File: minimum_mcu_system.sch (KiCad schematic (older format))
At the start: 0 parts

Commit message: resizing componentf
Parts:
- added U?: Stm8_my, symbol New_Schematic_Library:Stm8_my
- added Y?: Crystal, symbol Device:Crystal
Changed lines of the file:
@@
 Comment4 ""
 $EndDescr
+$Comp
+L New_Schematic_Library:Stm8_my U?
+U 1 1 606ACFA7
+P 5000 3550
+F 0 "U?" H 5008 4375 50  0000 C CNN
+F 1 "Stm8_my" H 5008 4284 50  0000 C CNN
+F 2 "" H 4550 4200 50  0001 C CNN
+F 3 "" H 4550 4200 50  0001 C CNN
+	1    5000 3550
+	1    0    0    -1
+$EndComp
+$Comp
+L Device:Crystal Y?
+U 1 1 606AE228
+P 3450 4050
+F 0 "Y?" V 3404 4181 50  0000 L CNN
+F 1 "Crystal" V 3495 4181 50  0000 L CNN
+F 2 "" H 3450 4050 50  0001 C CNN
+F 3 "~" H 3450 4050 50  0001 C CNN
+	1    3450 4050
+	0    1    1    0
+$EndComp
 $EndSCHEMATC

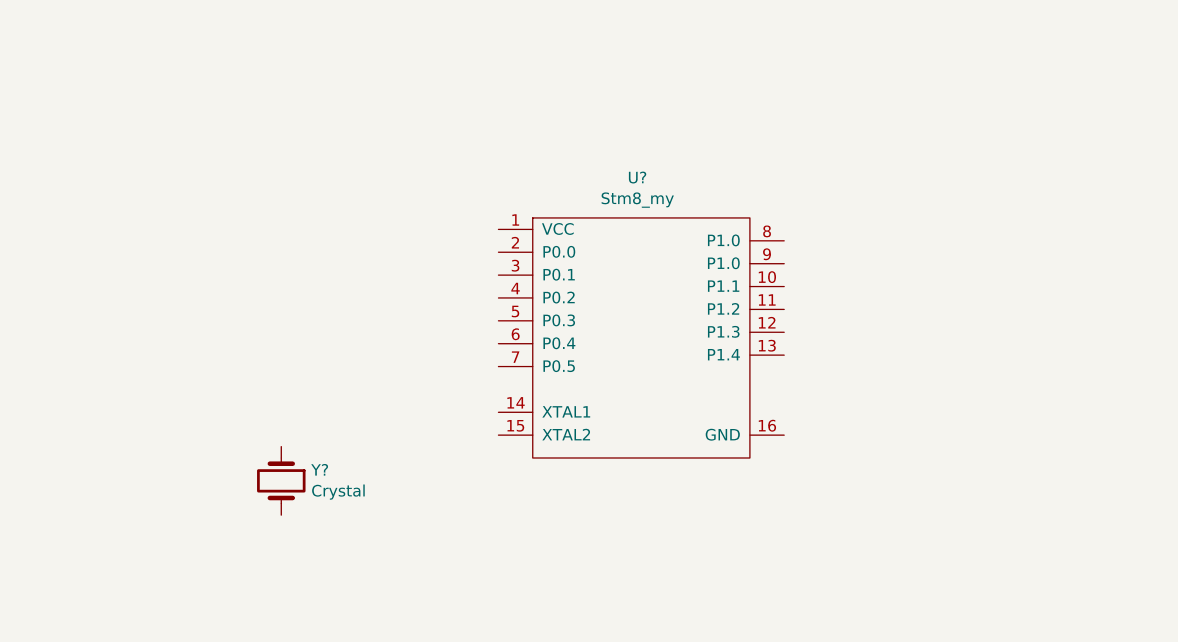
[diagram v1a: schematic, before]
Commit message: Added 3 capacitors,a cristal,an LED and a power input
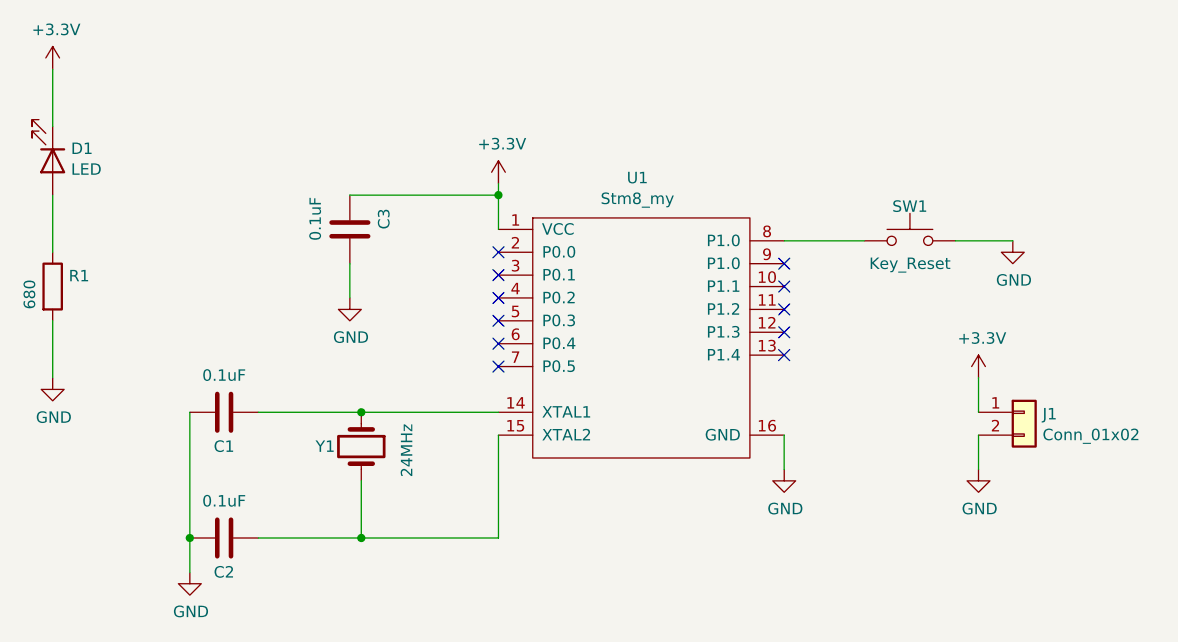
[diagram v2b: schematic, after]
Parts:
- added C1, C2, C3: 0.1uF, symbol Device:C
- added D1: LED, symbol Device:LED
- added J1: Conn_01x02, symbol Connector_Generic:Conn_01x02
- added R1: 680, symbol Device:R
- added SW1: Key_Reset, symbol Switch:SW_Push
- Y1: renamed from Y?; value Crystal -> 24MHz
- gave numbers to parts that had none: 1
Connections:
- net +3V3: now reaches U1.1 (VCC)
- net +3V3: now also C3.2, D1.1 (K), J1.1 (Pin_1)
- net at U1.14 (XTAL1): now also Y1.1, C1.1
- net at U1.15 (XTAL2): now also Y1.2, C2.1
- net GND: now reaches U1.16 (GND)
- net GND: now also C1.2, C2.2, C3.1, J1.2 (Pin_2), R1.2, SW1.2
- net at U1.8 (P1.0): now also SW1.1
- new net: D1.2 (A), R1.1
- no-connect marks 0 -> 11
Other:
- moved on the sheet: Y1
